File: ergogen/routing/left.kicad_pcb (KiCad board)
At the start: 2 copper layers, 177.3 x 122.5 mm, 130 parts, among them IC1 BQ24075RGTR, IC2 XC6220B331MR-G, J1 USB, J2 BAT, J3 SWD, SW1 RESET, SW2 POWER, Y1 32.768kHz

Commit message: feat(ergogen): the left half's matrix, autorouted
route.py matrix: columns socket to socket, each socket to its diode and
rows diode to diode, 0 DRC errors, 35 vias, columns mostly on the back
and rows on the front. Home's diode (D34) is left unrouted: at the
default spot on its turned key it sits against the board's outer edge,
where Freerouting can't reach either pad.

Co-Authored-By: Claude Opus 5.5 <noreply@anthropic.com>
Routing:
- net row4: track 0.00 -> 228.7 mm, vias 0 -> 7
- net row0: track 0.00 -> 152.3 mm, vias 0 -> 6
- net row1: track 0.00 -> 148.3 mm, vias 0 -> 7
- net row2: track 0.00 -> 145.6 mm, vias 0 -> 5
- net col6: track 0.00 -> 118.2 mm
- net row3: track 0.00 -> 116.1 mm, vias 0 -> 6
- net col5: track 0.00 -> 100.8 mm
- net col0: track 0.00 -> 85.8 mm, vias 0 -> 2
- net col4: track 0.00 -> 84.2 mm
- net col2: track 0.00 -> 81.6 mm
- net col3: track 0.00 -> 76.4 mm
- net col1: track 0.00 -> 60.8 mm
- net matrix_extra_home: track 0.00 -> 15.9 mm, vias 0 -> 2
- net matrix_inner_bottom: track 0.00 -> 14.5 mm
- net matrix_extra_num: track 0.00 -> 9.96 mm
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
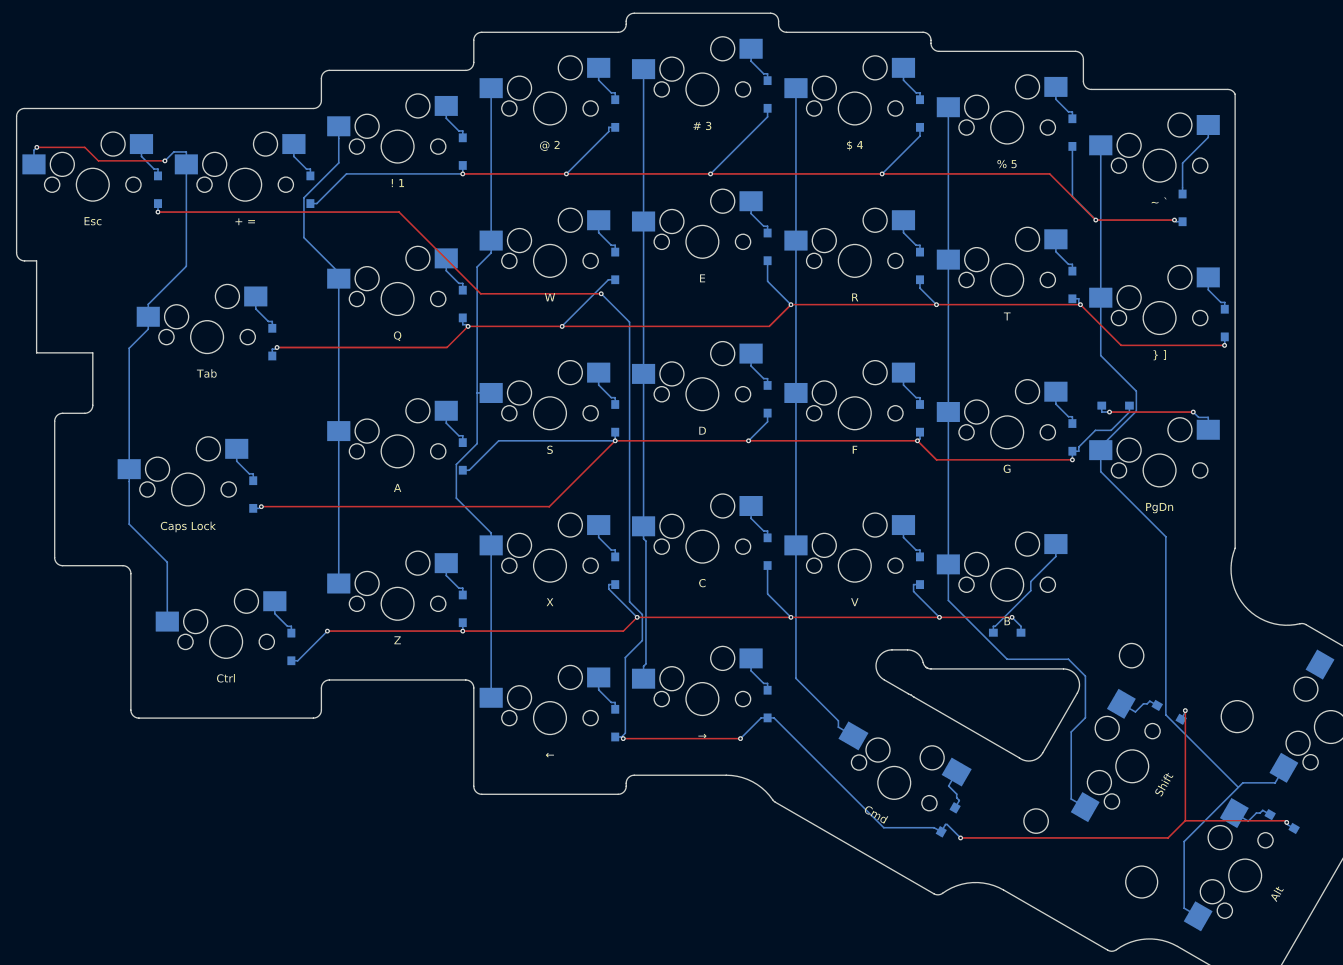
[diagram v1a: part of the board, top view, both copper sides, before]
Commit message: feat(ergogen): rip up the left half's matrix routing
It was routed with nothing else on the board and runs where the module
and power parts go. Parts get placed first now, then routed by section,
most constrained first.

Co-Authored-By: Claude Opus 5.5 <noreply@anthropic.com>
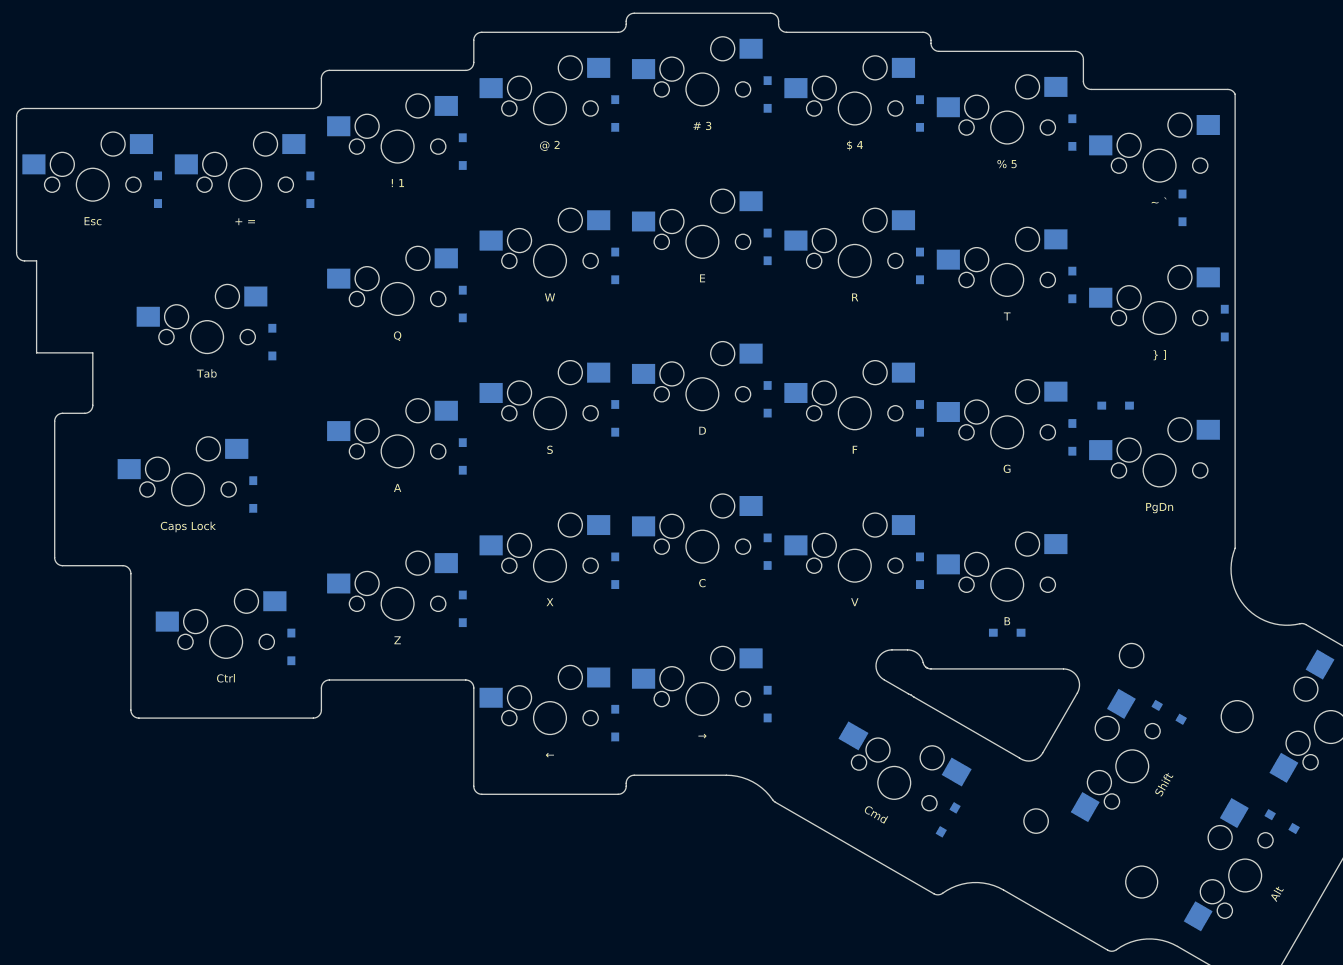
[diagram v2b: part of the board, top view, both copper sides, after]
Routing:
- net row4: track 228.7 -> 0.00 mm, vias 7 -> 0
- net row0: track 152.3 -> 0.00 mm, vias 6 -> 0
- net row1: track 148.3 -> 0.00 mm, vias 7 -> 0
- net row2: track 145.6 -> 0.00 mm, vias 5 -> 0
- net col6: track 118.2 -> 0.00 mm
- net row3: track 116.1 -> 0.00 mm, vias 6 -> 0
- net col5: track 100.8 -> 0.00 mm
- net col0: track 85.8 -> 0.00 mm, vias 2 -> 0
- net col4: track 84.2 -> 0.00 mm
- net col2: track 81.6 -> 0.00 mm
- net col3: track 76.4 -> 0.00 mm
- net col1: track 60.8 -> 0.00 mm
- net matrix_extra_home: track 15.9 -> 0.00 mm, vias 2 -> 0
- net matrix_inner_bottom: track 14.5 -> 0.00 mm
- net matrix_extra_num: track 9.96 -> 0.00 mm
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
